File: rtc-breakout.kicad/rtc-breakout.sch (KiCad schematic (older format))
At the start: 3 parts, among them J1 Pi, J2 RTC, SW1 SW_Push

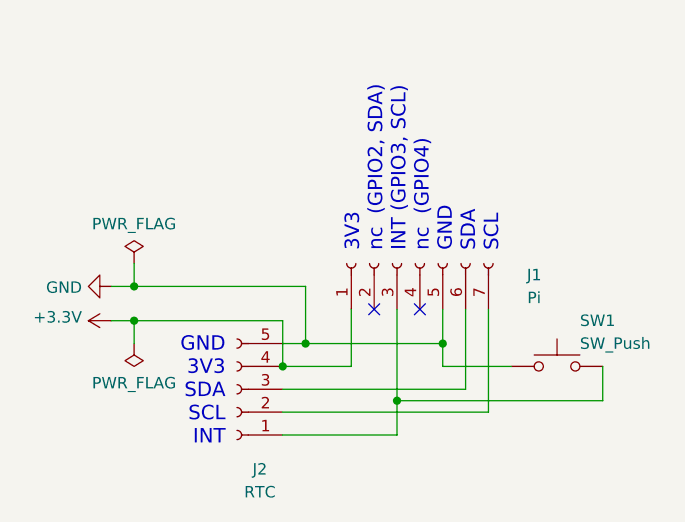
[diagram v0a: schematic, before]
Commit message: updated labels
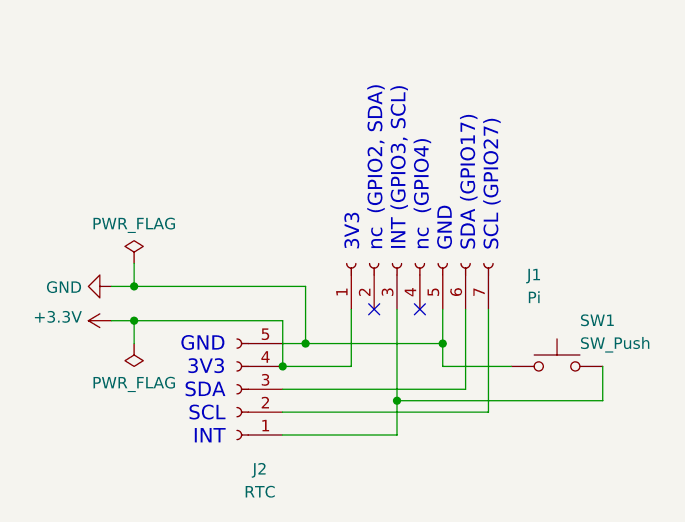
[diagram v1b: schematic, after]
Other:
- note added: "3V3\nnc (GPIO2, SDA)\nINT (GPIO3, SCL)\nnc (GPIO4)\nGND\nSDA (GPIO17)\nSCL (GPIO27)"
- note removed: "3V3\nnc (GPIO2, SDA)\nINT (GPIO3, SCL)\nnc (GPIO4)\nGND\nSDA\nSCL"
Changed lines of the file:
@@
 Sheet 1 1
 Title "RTC-Breakout Connector for a Raspberry Pi"
-Date "2020-06-16"
-Rev "1"
+Date "2020-06-25"
+Rev "1b"
 Comp "Bernhard Bablok"
 Comment1 "https://github.com/bablokb/pcb-rtc-breakout"
@@
 GND\n3V3\nSDA\nSCL\nINT
 Text Notes 4000 1900 1    63   ~ 0
-3V3\nnc  (GPIO2, SDA)\nINT (GPIO3, SCL)\nnc  (GPIO4)\nGND\nSDA\nSCL
+3V3\nnc  (GPIO2, SDA)\nINT (GPIO3, SCL)\nnc  (GPIO4)\nGND\nSDA (GPIO17)\nSCL (GPIO27)
 Wire Wire Line
 	3050 2300 3150 2300
